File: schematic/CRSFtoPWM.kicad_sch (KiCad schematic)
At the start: 29 parts, among them IC1 AP7375-50W5-7, IC2 ATSAMD21E18A-MU, IC3 SN74AUP1G04DBVR, IC4 MS563702BA03-50, J1 UART1/Rx, J2 UART2/GPS/CLI, J3 ICSP, J4 I2C, J5 SBus, J6 TSW-104-08-G-T-RA, J7 TSW-104-08-G-T-RA, U1 AP2210N-3.3TRG1

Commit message: Changed ICSP pullups
per datasheet
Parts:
- added J1: Bat+, symbol Connector_Generic:Conn_01x01
- added J2: Bat-, symbol Connector_Generic:Conn_01x01
- C8, C9: value C -> 100nF
- R3: value 100K -> 1K
- renumbered J1 to J3, J2 to J4, J3 to J5, J4 to J6, J5 to J7, J6 to J8, J7 to J9
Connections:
- net +3V3: now also R3.1; no longer R3.2
- net GND: now also J2.1 (Pin_1)
- net Vbat: now also J1.1 (Pin_1)
- net at IC2.26 (RESETN), J5.1 (Pin_1): no longer R3.1
- net at IC2.31 (PA30), J5.4 (Pin_4): now also R3.2

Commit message: Added two more outputs
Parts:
- added J10: CH9, symbol Connector_Generic:Conn_01x03
- added J11: CH10, symbol Connector_Generic:Conn_01x03
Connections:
- net GND: now also J10.3 (Pin_3), J11.3 (Pin_3)
- net Vservo: now also J10.2 (Pin_2), J11.2 (Pin_2)
- net CH9: now reaches IC2.23 (PA24)
- net CH9: now also J10.1 (Pin_1)
- net CH10: now reaches IC2.24 (PA25)
- net CH10: now also J11.1 (Pin_1)
- no-connect marks 7 -> 5

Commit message: Footprints assigned
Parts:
- C8, C9: footprint (none) -> Capacitor_SMD:C_0402_1005Metric
- D1: footprint (none) -> LED_SMD:LED_0603_1608Metric
- IC3: footprint SOT95P280X145-5N -> SamacSys_Parts2:SOT95P280X145-5N
- IC4: footprint MS5637_1 -> SamacSys_Parts2:MS5637_1
- J1, J2: footprint (none) -> Connector_PinHeader_2.54mm:PinHeader_1x01_P2.54mm_Vertical
- J10, J11, J7: footprint (none) -> Connector_PinHeader_2.54mm:PinHeader_1x03_P2.54mm_Vertical
- J3, J4, J6: footprint (none) -> Connector_PinHeader_2.54mm:PinHeader_1x04_P2.54mm_Vertical
- J5: footprint (none) -> Connector_PinHeader_2.54mm:PinHeader_1x05_P2.54mm_Vertical
- R1, R2, R3, R4, R5, R6: footprint (none) -> Resistor_SMD:R_0603_1608Metric

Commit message: Updated some footprints
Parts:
- J8, J9: footprint SamacSys Parts:HDRRA12W64P254_3X4_1016X254X810P -> SamacSys_Parts:HDRRA12W64P254_3X4_1016X254X810P
- U1: footprint SamacSys Parts:SOT95P280X145-3N -> SamacSys_Parts:SOT95P280X145-3N
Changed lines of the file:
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@@
       (effects (font (size 1.27 1.27)) hide)
     )
-    (property "Footprint" "SamacSys Parts:HDRRA12W64P254_3X4_1016X254X810P" (id 2) (at 242.57 46.355 0)
+    (property "Footprint" "SamacSys_Parts:HDRRA12W64P254_3X4_1016X254X810P" (id 2) (at 242.57 46.355 0)
       (effects (font (size 1.27 1.27)) (justify left) hide)
     )
@@
       (effects (font (size 1.27 1.27)) hide)
     )
-    (property "Footprint" "SamacSys Parts:HDRRA12W64P254_3X4_1016X254X810P" (id 2) (at 242.57 74.295 0)
+    (property "Footprint" "SamacSys_Parts:HDRRA12W64P254_3X4_1016X254X810P" (id 2) (at 242.57 74.295 0)
       (effects (font (size 1.27 1.27)) (justify left) hide)
     )
@@
     (property "Reference" "U1" (id 0) (at 59.69 125.6243 0))
     (property "Value" "AP2210N-3.3TRG1" (id 1) (at 59.69 128.3994 0))
-    (property "Footprint" "SamacSys Parts:SOT95P280X145-3N" (id 2) (at 49.53 137.16 0)
+    (property "Footprint" "SamacSys_Parts:SOT95P280X145-3N" (id 2) (at 49.53 137.16 0)
       (effects (font (size 1.27 1.27)) (justify left) hide)
     )
@@
     )
     (path "/ac11a4ab-e224-47ec-9e1c-78820c399ce4"
-      (reference "J8") (unit 1) (value "TSW-104-08-G-T-RA") (footprint "SamacSys Parts:HDRRA12W64P254_3X4_1016X254X810P")
+      (reference "J8") (unit 1) (value "TSW-104-08-G-T-RA") (footprint "SamacSys_Parts:HDRRA12W64P254_3X4_1016X254X810P")
     )
     (path "/dd3bb852-f13c-4c62-9d02-ca2b65859266"
-      (reference "J9") (unit 1) (value "TSW-104-08-G-T-RA") (footprint "SamacSys Parts:HDRRA12W64P254_3X4_1016X254X810P")
+      (reference "J9") (unit 1) (value "TSW-104-08-G-T-RA") (footprint "SamacSys_Parts:HDRRA12W64P254_3X4_1016X254X810P")
     )
     (path "/7459503b-d174-4f7c-8819-82edcacdb623"
@@
     )
     (path "/fc625155-88c3-48a5-9c0e-032f9cbc65db"
-      (reference "U1") (unit 1) (value "AP2210N-3.3TRG1") (footprint "SamacSys Parts:SOT95P280X145-3N")
-    )
-  )
+      (reference "U1") (unit 1) (value "AP2210N-3.3TRG1") (footprint "SamacSys_Parts:SOT95P280X145-3N")
+    )
+  )

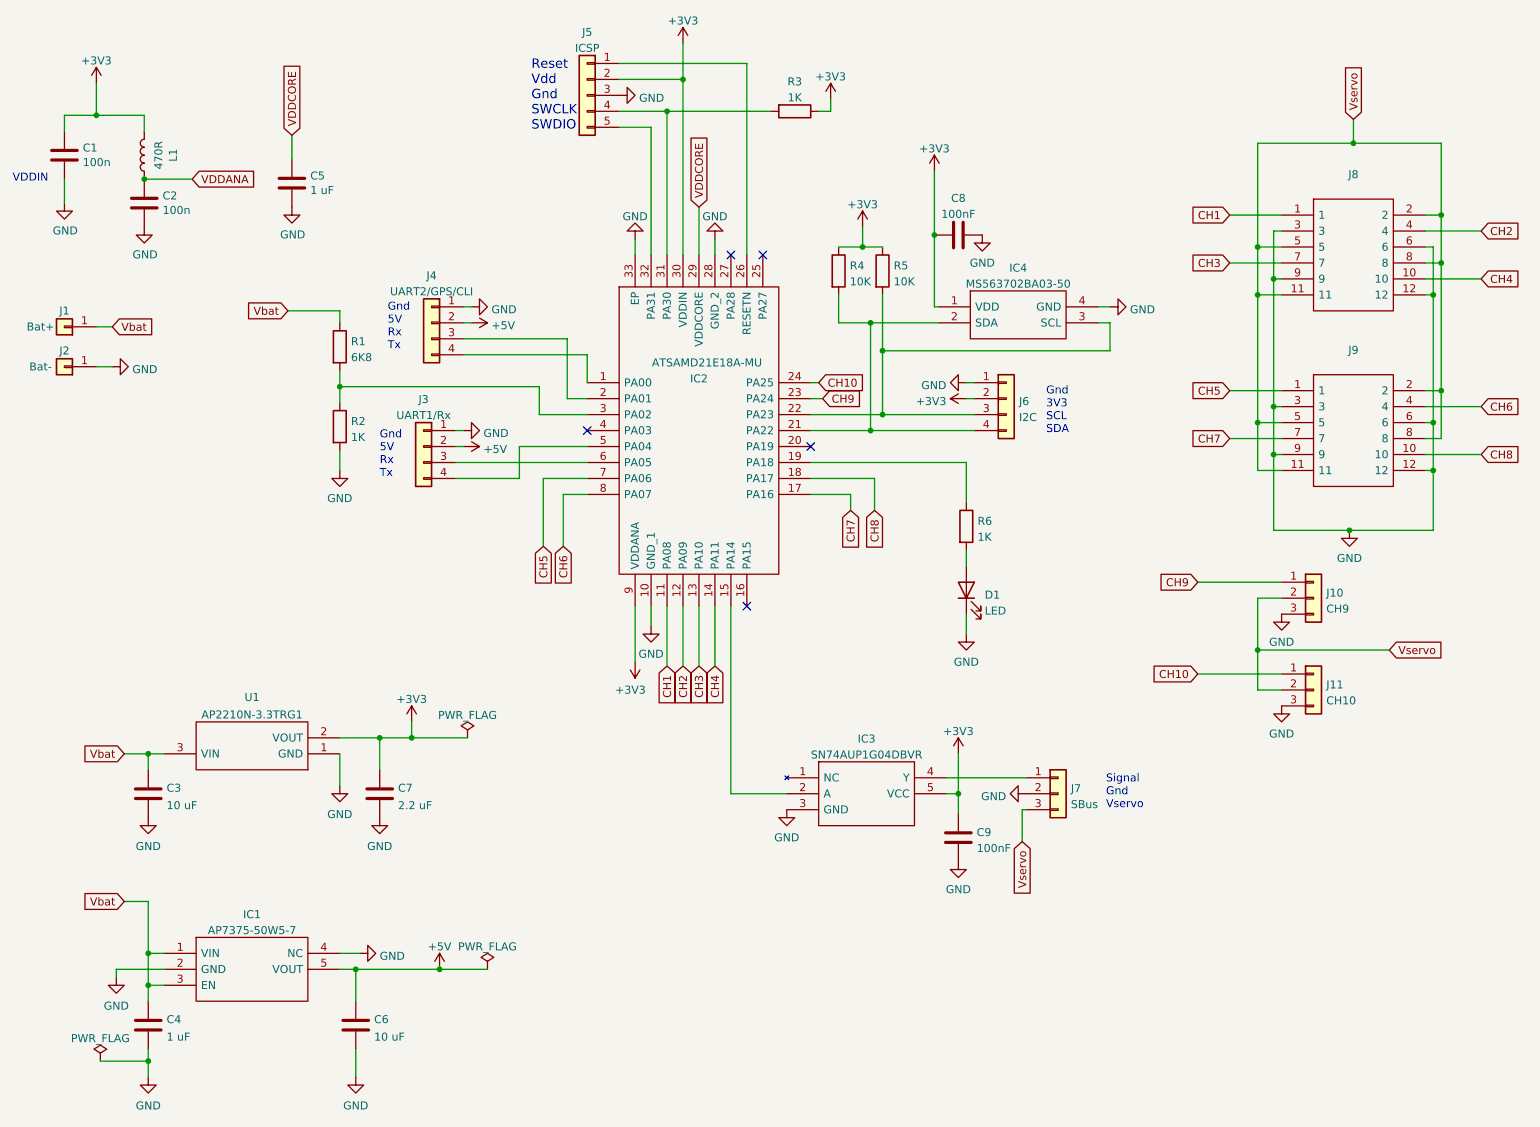
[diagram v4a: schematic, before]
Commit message: Changed connections to improve pcb layout
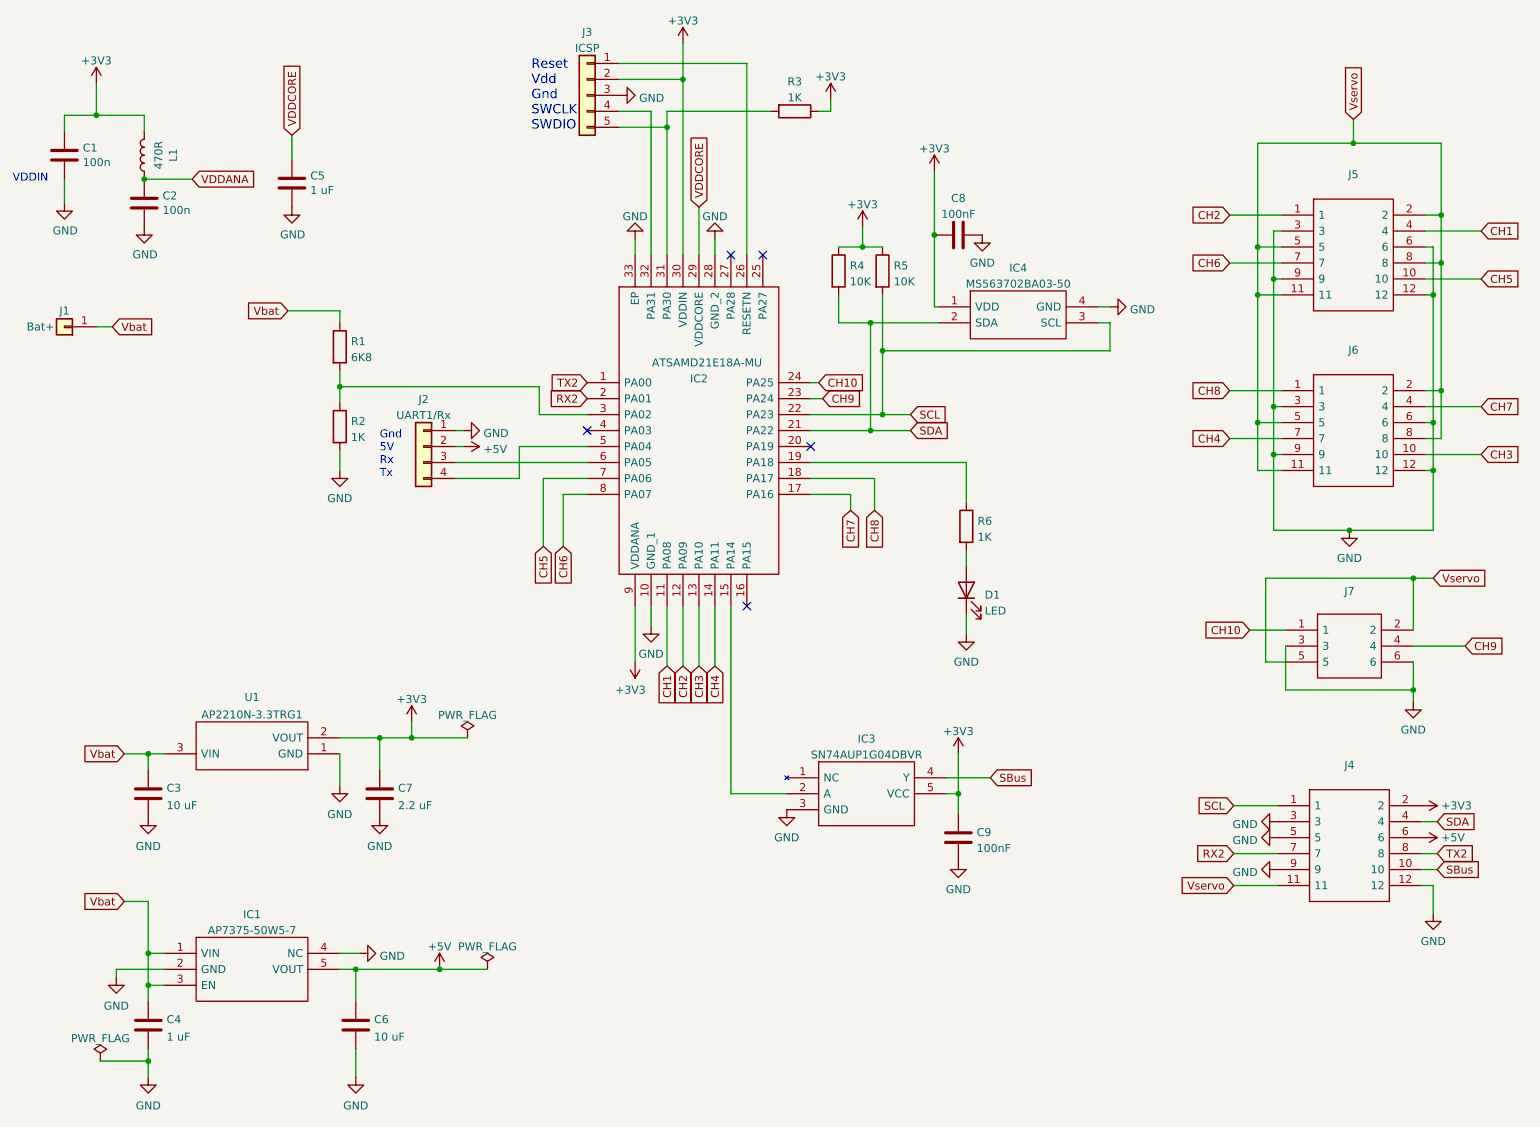
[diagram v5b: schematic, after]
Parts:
- removed J10: CH9, Connector_PinHeader_2.54mm:PinHeader_1x03_P2.54mm_Vertical, symbol Connector_Generic:Conn_01x03
- removed J11: CH10, Connector_PinHeader_2.54mm:PinHeader_1x03_P2.54mm_Vertical, symbol Connector_Generic:Conn_01x03
- removed J2: Bat-, Connector_PinHeader_2.54mm:PinHeader_1x01_P2.54mm_Vertical, symbol Connector_Generic:Conn_01x01
- removed J4: UART2/GPS/CLI, Connector_PinHeader_2.54mm:PinHeader_1x04_P2.54mm_Vertical, symbol Connector_Generic:Conn_01x04
- removed J6: I2C, Connector_PinHeader_2.54mm:PinHeader_1x04_P2.54mm_Vertical, symbol Connector_Generic:Conn_01x04
- removed J7: SBus, Connector_PinHeader_2.54mm:PinHeader_1x03_P2.54mm_Vertical, symbol Connector_Generic:Conn_01x03
- added J4: TSW-104-08-G-T-RA, SamacSys_Parts:HDRRA12W64P254_3X4_1016X254X810P, symbol SamacSys_Parts:TSW-104-08-G-T-RA
- added J7: TSW-102-08-L-T-RA, SamacSys_Parts:HDRRA6W64P254_3X2_508X254X810P, symbol SamacSys_Parts:TSW-102-08-L-T-RA
- renumbered J3 to J2, J5 to J3, J8 to J5, J9 to J6
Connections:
- net +3V3: now also J4.2
- net +5V: now also J4.6
- net CH1: now also J5.4; no longer J5.1
- net CH10: now also J7.1
- net CH2: now also J5.1; no longer J5.4
- net CH3: now also J6.10; no longer J5.7
- net CH4: now also J6.7; no longer J5.10
- net CH5: now also J5.10; no longer J6.1
- net CH6: now also J5.7; no longer J6.4
- net CH7: now also J6.4; no longer J6.7
- net CH8: now also J6.1; no longer J6.10
- net CH9: now also J7.4
- net GND: now also J4.12, J4.3, J4.5, J4.9, J7.3, J7.6
- net Vservo: now also J4.11, J7.2, J7.5
- net SBus: now reaches IC3.4 (Y)
- net SBus: now also J4.10
- net SCL: now reaches IC2.22 (PA23), IC4.3 (SCL), R5.2
- net SCL: now also J4.1
- net SDA: now reaches IC2.21 (PA22), IC4.2 (SDA), R4.2
- net SDA: now also J4.4
- net at IC2.31 (PA30), R3.2: now also J3.5 (Pin_5); no longer J3.4 (Pin_4)
- net at IC2.32 (PA31): now also J3.4 (Pin_4); no longer J3.5 (Pin_5)
- net TX2: now reaches IC2.1 (PA00)
- net TX2: now also J4.8
- net RX2: now reaches IC2.2 (PA01)
- net RX2: now also J4.7
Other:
- note removed: "Gnd 3V3 SCL SDA"
- note removed: "Signal Gnd Vservo"

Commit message: Initial pcb parts layout
Also fixed VDDANA
Made some schematic changes to improve layout
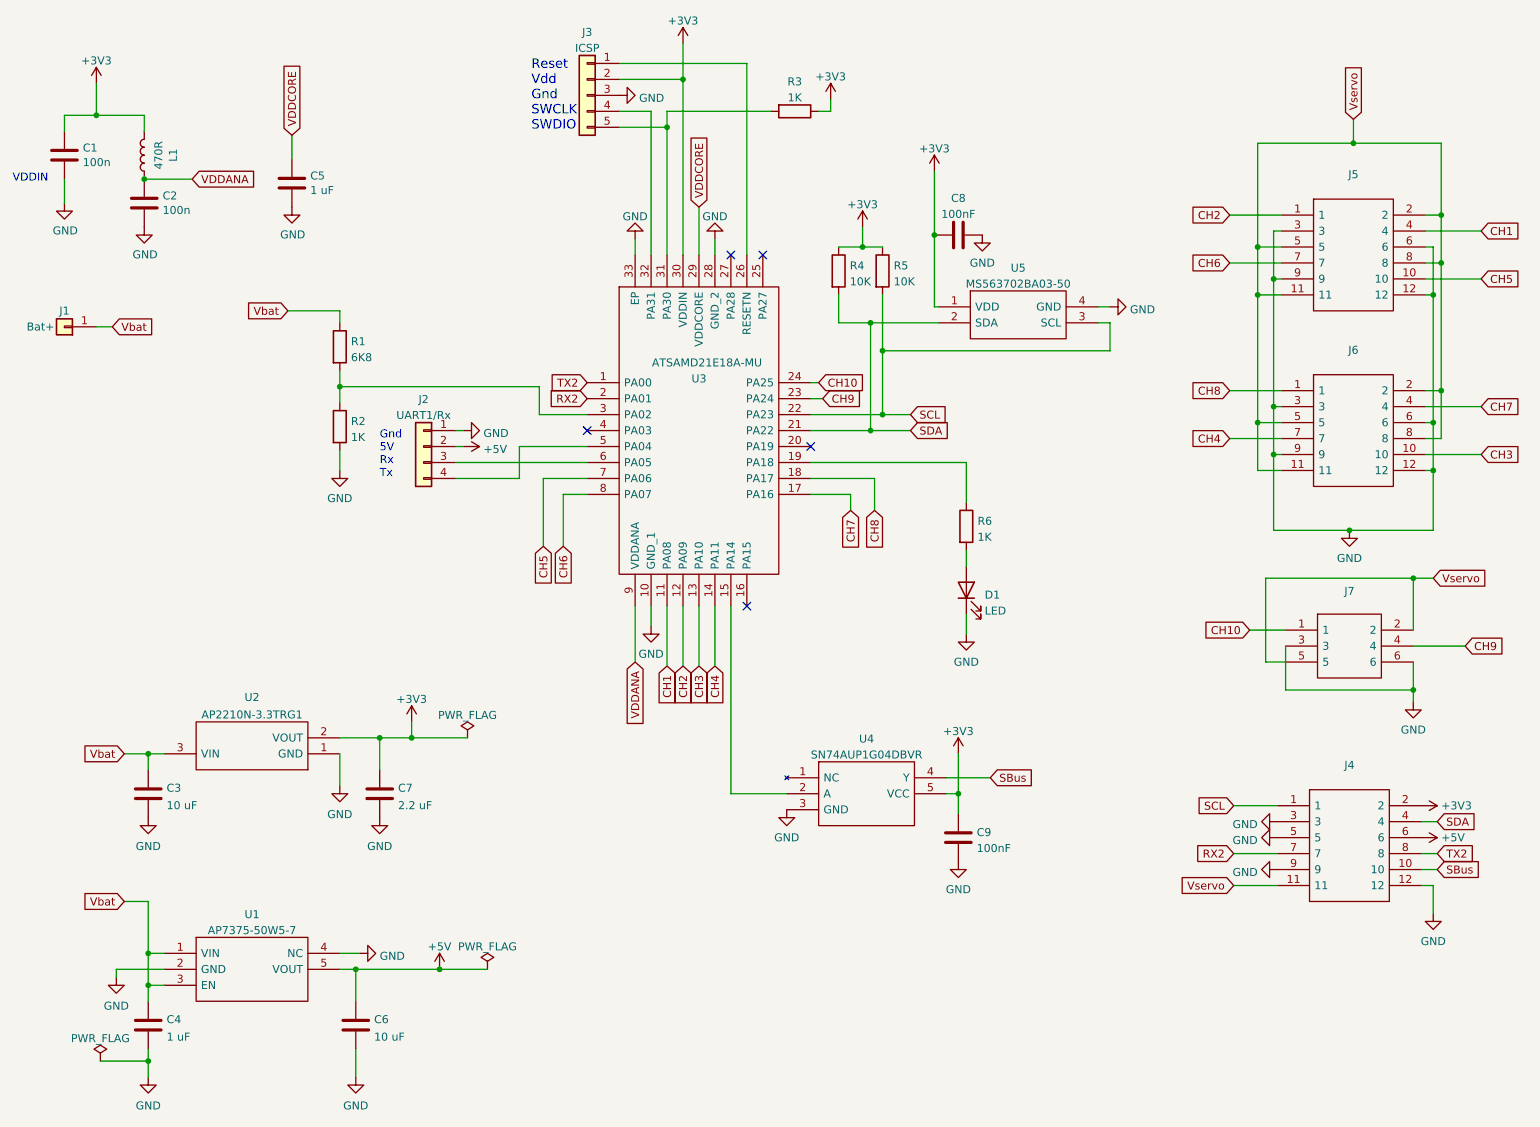
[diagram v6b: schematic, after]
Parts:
- renumbered IC1 to U1, U1 to U2, IC2 to U3, IC3 to U4, IC4 to U5
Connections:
- net +3V3: no longer U3.9 (VDDANA)
- net VDDANA: now also U3.9 (VDDANA)

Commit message: Pcb fully routed - needs optimization
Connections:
- net +3V3: now also J4.1; no longer J4.2
- net +5V: now also J4.2; no longer J4.6
- net GND: now also J4.6; no longer J4.5
- net RX2: now also J4.5; no longer J4.7
- net SCL: now also J4.7; no longer J4.1
- net SDA: now also J4.8; no longer J4.4
- net TX2: now also J4.4; no longer J4.8
- net at R6.1: now also U3.16 (PA15); no longer U3.19 (PA18)
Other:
- moved on the sheet: D1, R6

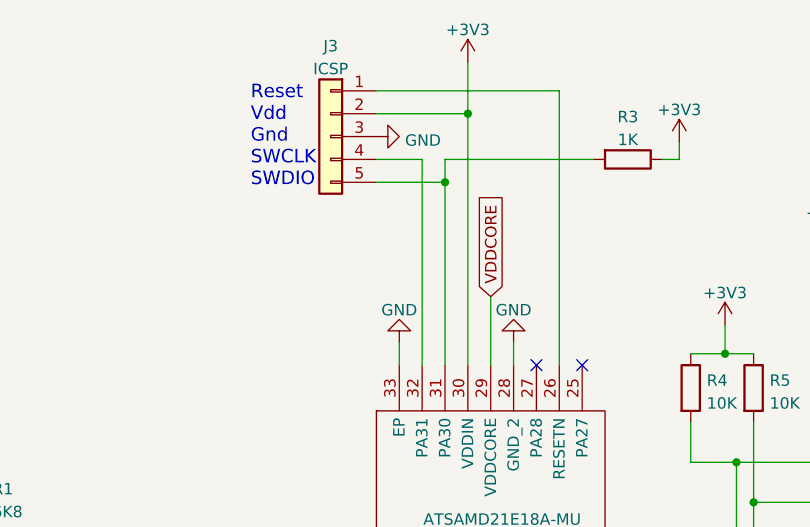
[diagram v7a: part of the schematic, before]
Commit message: Smaller pcb and tweaks
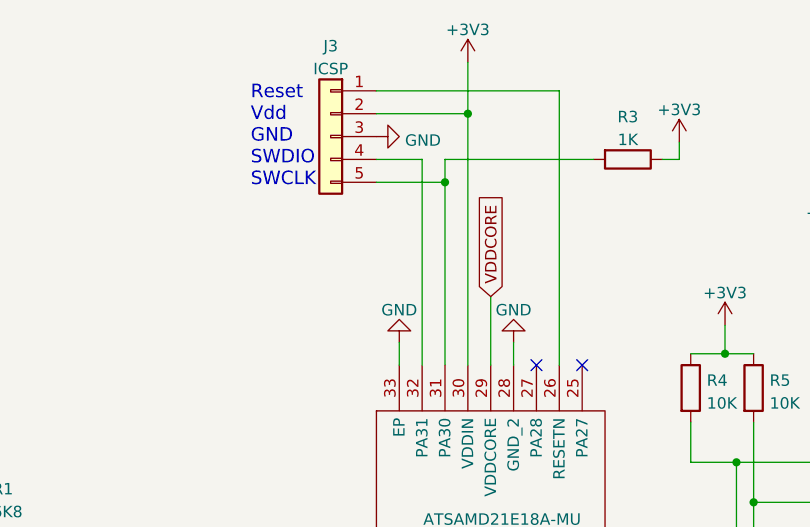
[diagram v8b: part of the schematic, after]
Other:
- note added: "Reset Vdd GND SWDIO SWCLK"
- note removed: "Reset Vdd Gnd SWCLK SWDIO"
